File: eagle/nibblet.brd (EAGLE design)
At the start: 31.3 x 31.2 mm, 21 parts, among them IC1 MEGA8-AI

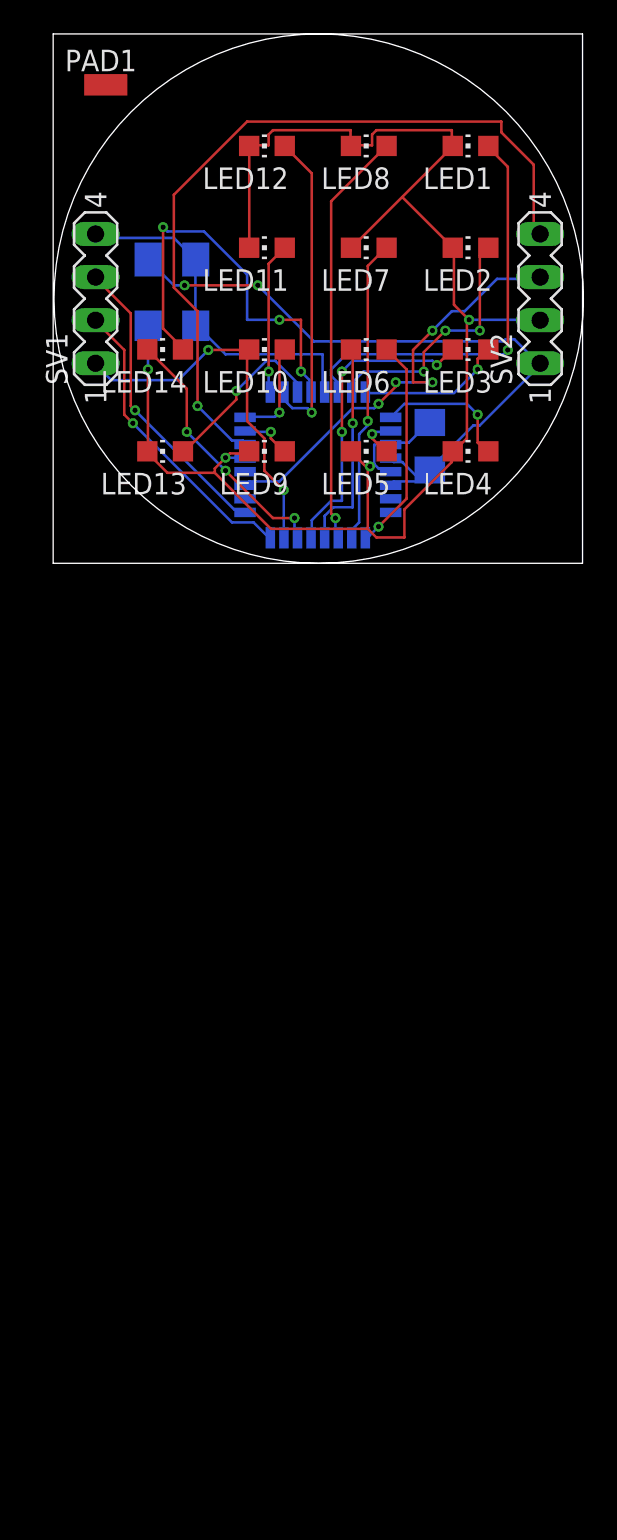
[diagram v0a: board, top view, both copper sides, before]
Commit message: add series resistors to leds
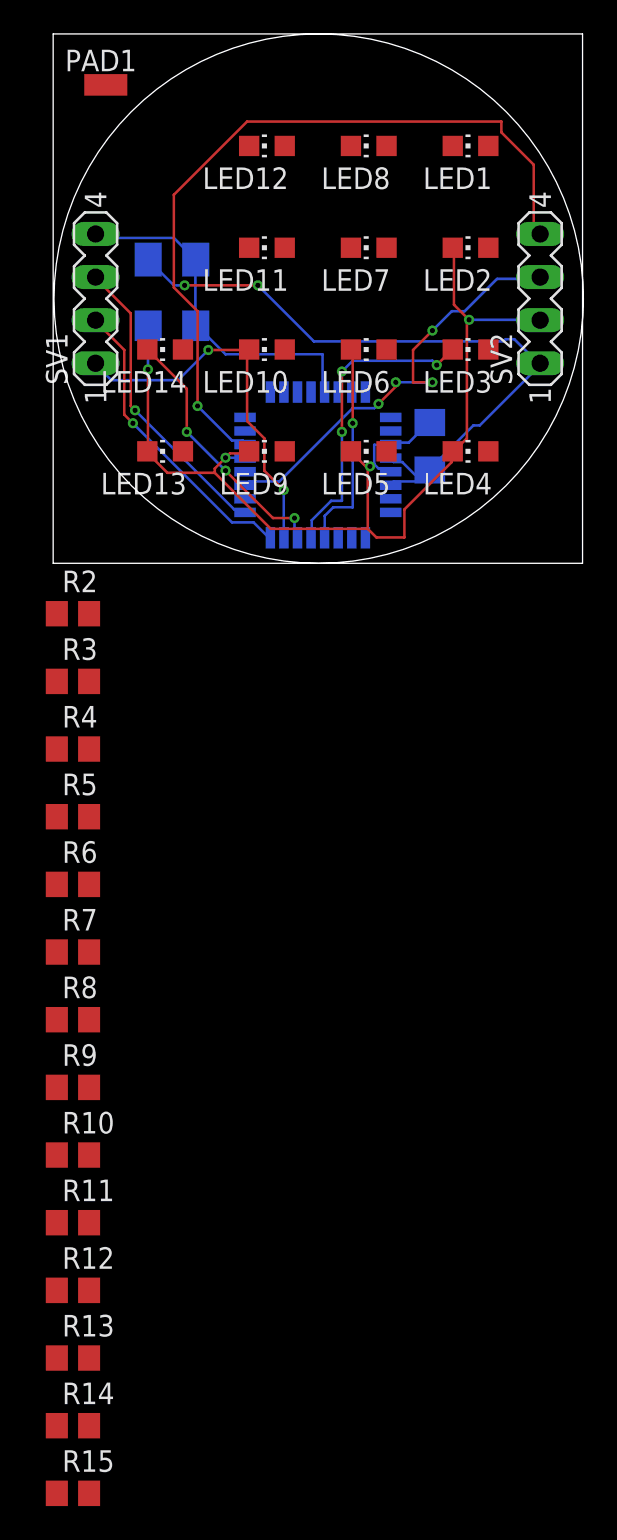
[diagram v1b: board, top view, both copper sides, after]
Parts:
- added R10, R11, R12, R13, R14, R15, R2, R3, R4, R5, R6, R7, R8, R9: (no value), rcl:R0805
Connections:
- new net N$17: IC1.11, R9.1
- new net N$18: LED8.C, R9.2
- new net N$25: LED7.C, R8.2
- new net N$26: LED6.C, R7.2
- new net N$27: LED5.C, R6.2
- new net N$28: LED4.C, R5.2
- new net N$29: LED3.C, R4.2
- new net N$30: LED2.C, R3.2
- new net N$31: LED1.C, R2.2
- new net N$32: LED13.C, R14.2
- new net N$33: IC1.28, R15.1
- new net N$34: LED14.C, R15.2
- new net N$35: LED10.C, R11.2
- new net N$36: LED9.C, R10.2
- net GND: now also LED1.A, LED11.A, LED12.A, LED13.A, LED2.A, LED4.A, LED5.A, LED7.A, LED8.A, LED9.A; no longer LED1.C, LED11.C, LED12.C, LED13.C, LED2.C, LED4.C, LED5.C, LED7.C, LED8.C, LED9.C
- net N$1: now also IC1.25, R12.1; no longer IC1.23, LED9.A
- net N$10: now also IC1.32, R4.1; no longer IC1.1, LED4.A
- net N$11: now also IC1.1, R5.1; no longer IC1.2, LED5.A
- net N$12: now also IC1.2, R6.1; no longer IC1.9, LED6.A
- net N$13: now also IC1.9, R7.1; no longer IC1.10, LED7.A
- net N$14: now also IC1.10, R8.1; no longer IC1.11, LED8.A
- net N$15: now also LED10.A; no longer LED10.C
- net N$2: now also LED11.C, R12.2; no longer IC1.24, LED10.A
- net N$20: now also LED14.A; no longer LED14.C
- net N$22: now also LED3.A; no longer LED3.C
- net N$23: now also LED6.A; no longer LED6.C
- net N$3: now also IC1.23, R10.1; no longer IC1.25, LED11.A
- net N$4: now also IC1.24, R11.1; no longer IC1.26, LED12.A
- net N$5: now also IC1.26, R13.1; no longer IC1.27, LED13.A
- net N$6: now also LED12.C, R13.2; no longer IC1.28, LED14.A
- net N$7: now also IC1.27, R14.1; no longer IC1.30, LED1.A
- net N$8: now also IC1.30, R2.1; no longer IC1.31, LED2.A
- net N$9: now also IC1.31, R3.1; no longer IC1.32, LED3.A
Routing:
- net GND: track 97.6 -> 62.7 mm
- net N$7: track 24.9 -> 0.00 mm, vias 1 -> 0
- net N$14: track 24.7 -> 0.00 mm, vias 1 -> 0
- net N$6: track 24.2 -> 0.00 mm, vias 3 -> 0
- net N$4: track 18.8 -> 0.00 mm, vias 1 -> 0
- net N$13: track 18.0 -> 0.00 mm, vias 1 -> 0
- net N$8: track 15.1 -> 0.00 mm, vias 3 -> 0
- net N$12: track 12.7 -> 0.00 mm, vias 1 -> 0
- net N$5: track 10.3 -> 0.00 mm, vias 1 -> 0
- net N$3: track 8.96 -> 0.00 mm, vias 1 -> 0
- net N$9: track 8.72 -> 0.00 mm, vias 1 -> 0
- net N$10: track 8.21 -> 0.00 mm, vias 1 -> 0
- net N$2: track 5.99 -> 0.00 mm, vias 1 -> 0
- net N$1: track 3.05 -> 0.00 mm, vias 1 -> 0
- net N$11: track 2.59 -> 0.00 mm, vias 1 -> 0

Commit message: placed resistors and autorouted 100%
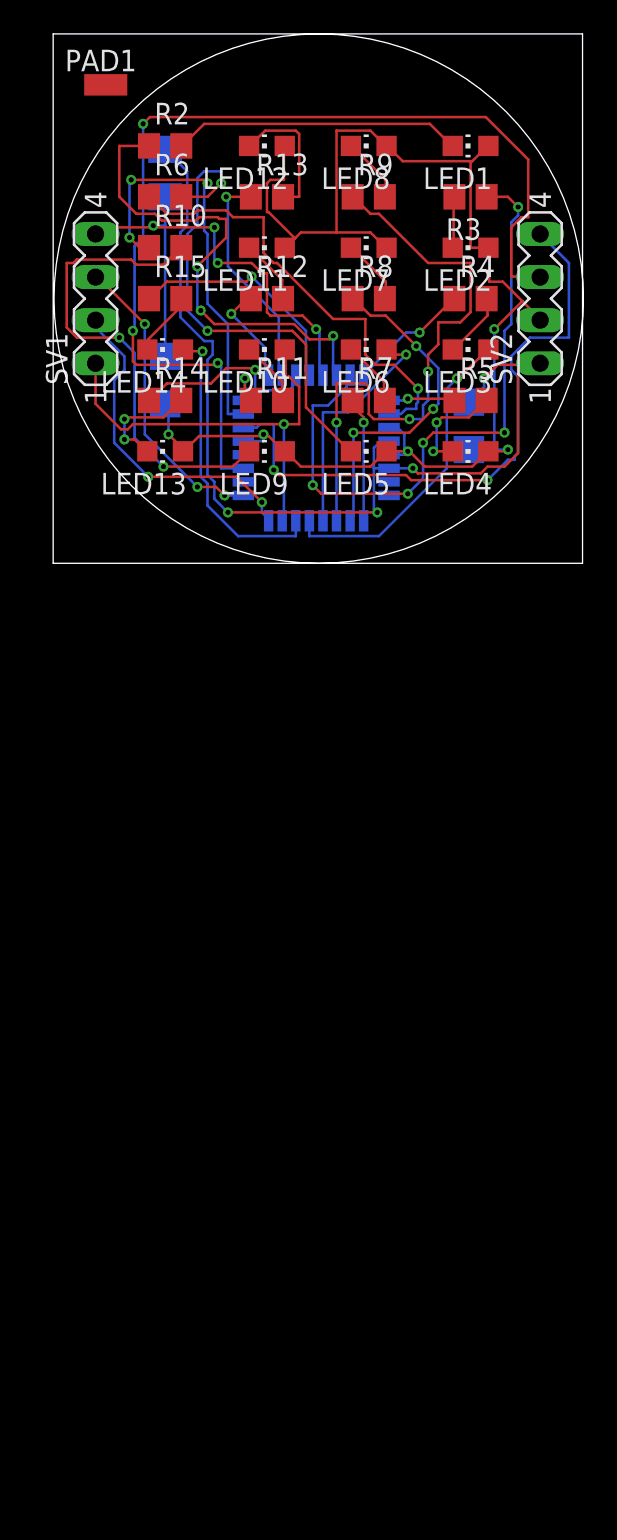
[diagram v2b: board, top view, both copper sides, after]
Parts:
- moved R15 70.6 mm to (6.60, 15.6)
- moved R13 69.4 mm to (12.6, 21.6)
- moved R14 60.7 mm to (6.60, 9.60)
- moved R12 59.6 mm to (12.6, 15.6)
- moved R9 55.3 mm to (18.6, 21.6)
- moved R10 53.7 mm to (6.60, 18.6)
- moved R11 49.8 mm to (12.6, 9.60)
- moved R8 45.9 mm to (18.6, 15.6)
- moved R6 40.9 mm to (6.60, 21.6)
- moved R3 36.9 mm to (24.6, 21.6), turned to 180 degrees
- moved R7 36.9 mm to (18.6, 9.60)
- moved R4 35.4 mm to (24.6, 15.6)
- moved R5 33.9 mm to (24.6, 9.60)
- moved R2 28.1 mm to (6.60, 24.6)
- moved R1 5.12 mm to (6.60, 23.0), turned to 270 degrees
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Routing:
- net N$9: track 0.00 -> 37.9 mm, vias 0 -> 5
- net N$17: track 0.00 -> 34.7 mm, vias 0 -> 3
- net N$19: track 26.0 -> 60.1 mm, vias 4 -> 3
- net N$8: track 0.00 -> 28.9 mm, vias 0 -> 3
- net N$36: track 0.00 -> 28.6 mm, vias 0 -> 2
- net N$27: track 0.00 -> 28.3 mm, vias 0 -> 2
- net N$12: track 0.00 -> 26.1 mm, vias 0 -> 1
- net N$3: track 0.00 -> 24.6 mm, vias 0 -> 3
- net GND: track 62.7 -> 83.6 mm, vias 4 -> 5
- net N$14: track 0.00 -> 19.8 mm, vias 0 -> 3
- net VCC: track 40.7 -> 58.7 mm, vias 2 -> 4
- net N$31: track 0.00 -> 17.1 mm
- net N$33: track 0.00 -> 13.8 mm, vias 0 -> 1
- net N$5: track 0.00 -> 13.3 mm, vias 0 -> 1
- net N$7: track 0.00 -> 11.3 mm, vias 0 -> 1
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
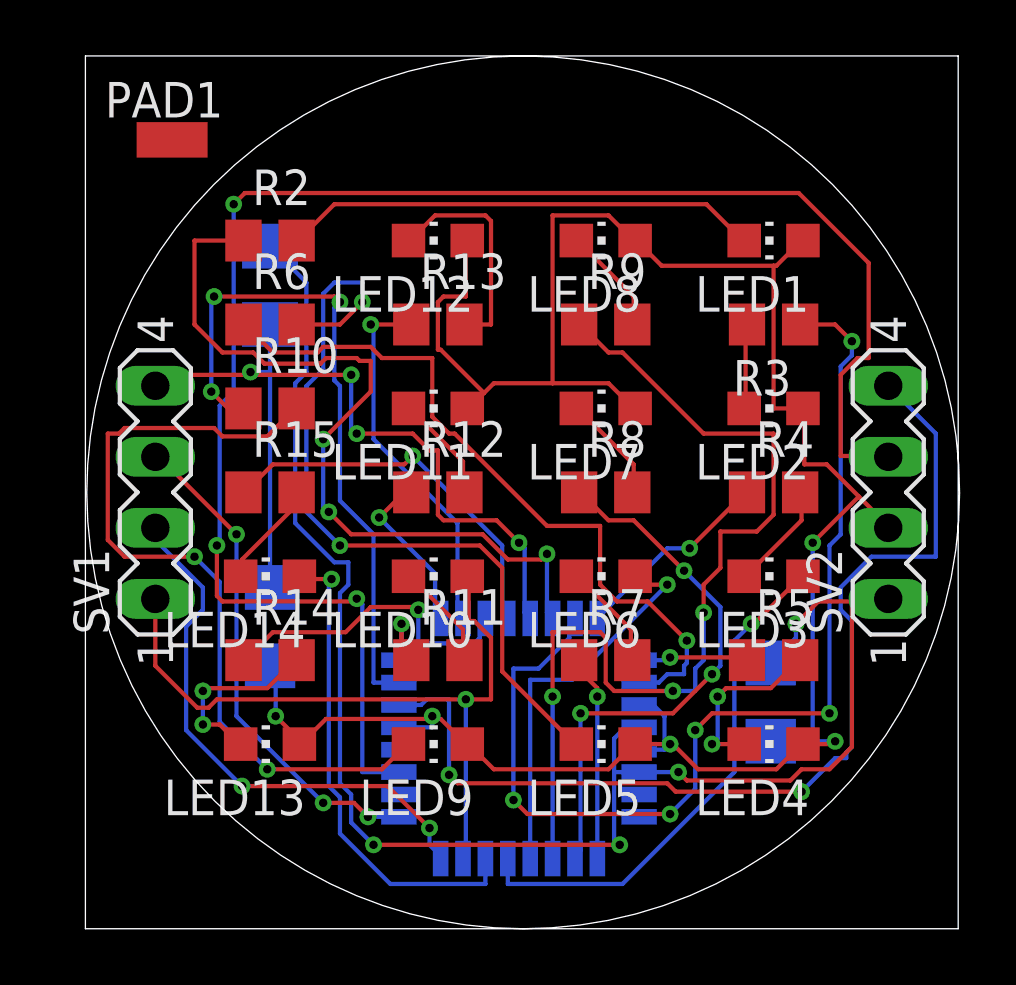
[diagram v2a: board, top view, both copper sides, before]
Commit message: consistent led order
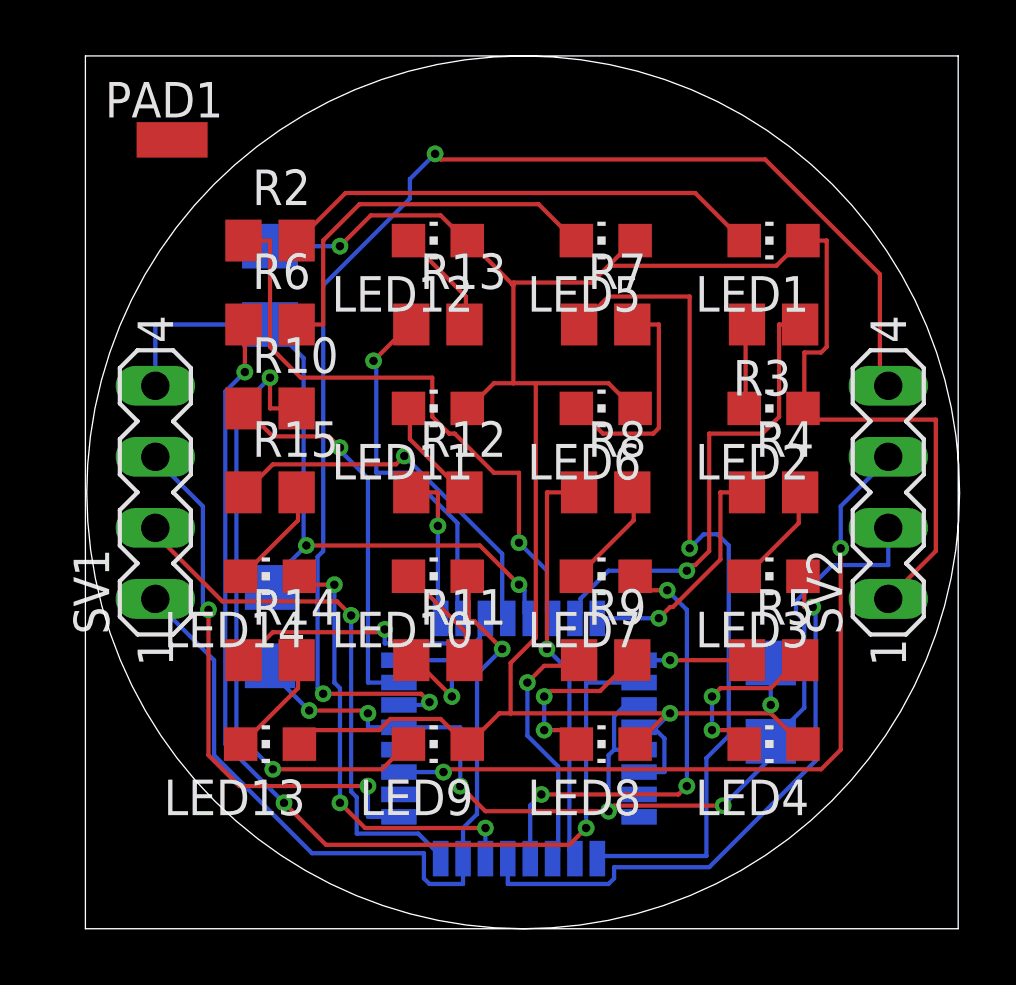
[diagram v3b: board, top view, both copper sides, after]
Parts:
- moved LED5 18.0 mm to (18.6, 24.6)
- moved LED8 18.0 mm to (18.6, 6.60)
- moved R7 12.0 mm to (18.6, 21.6)
- moved R9 12.0 mm to (18.6, 9.60)
- moved LED6 6.00 mm to (18.6, 18.6)
- moved LED7 6.00 mm to (18.6, 12.6)
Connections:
- net GND: no longer LED1.A, LED11.A, LED12.A, LED13.A, LED2.A, LED4.A, LED5.A, LED7.A, LED8.A, LED9.A
- net N$23: now also LED7.A; no longer LED6.A
- net VCC: now also LED1.A, LED11.A, LED12.A, LED13.A, LED2.A, LED4.A, LED5.A, LED6.A, LED8.A, LED9.A
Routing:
- net GND: track 83.6 -> 39.3 mm
- net VCC: track 58.7 -> 92.2 mm, vias 4 -> 3
- net N$19: track 60.1 -> 27.3 mm, vias 3 -> 2
- net N$17: track 34.7 -> 9.01 mm, vias 3 -> 1
- net N$13: track 7.39 -> 30.6 mm
- net N$9: track 37.9 -> 17.1 mm, vias 5 -> 1
- net N$27: track 28.3 -> 14.1 mm, vias 2 -> 0
- net N$16: track 36.5 -> 48.2 mm, vias 2 -> 3
- net N$12: track 26.1 -> 37.1 mm, vias 1 -> 3
- net N$3: track 24.6 -> 14.0 mm, vias 3 -> 1
- net N$8: track 28.9 -> 22.0 mm, vias 3 -> 1
- net N$36: track 28.6 -> 22.3 mm
- net N$14: track 19.8 -> 14.7 mm, vias 3 -> 1
- net N_RESET: track 31.2 -> 26.4 mm, vias 4 -> 2
- net N$15: track 25.8 -> 30.0 mm
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
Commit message: led position really consistent
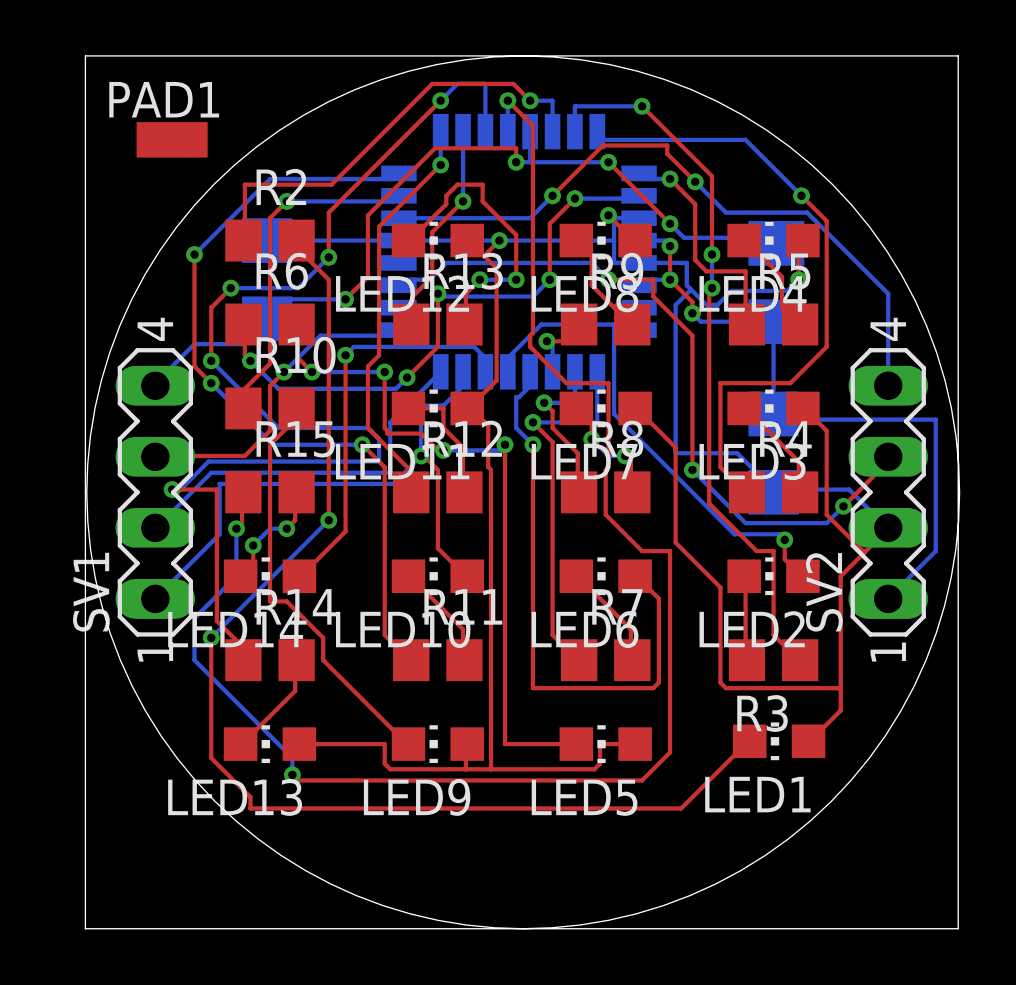
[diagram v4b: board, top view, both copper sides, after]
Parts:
- moved R1 18.1 mm to (24.7, 23.1), turned to 90 degrees
- moved LED4 18.0 mm to (24.6, 24.6)
- moved LED5 18.0 mm to (18.6, 6.60)
- moved LED8 18.0 mm to (18.6, 24.6)
- moved LED1 17.9 mm to (24.8, 6.70)
- moved IC1 17.4 mm to (15.5, 24.2)
- moved C2 12.4 mm to (6.50, 23.2), turned to 270 degrees
- moved R3 12.0 mm to (24.6, 9.60)
- moved R5 12.0 mm to (24.6, 21.6)
- moved R7 12.0 mm to (18.6, 9.60)
- moved R9 12.0 mm to (18.6, 21.6)
- moved C1 8.90 mm to (24.6, 17.0)
- moved LED2 6.00 mm to (24.6, 12.6)
- moved LED3 6.00 mm to (24.6, 18.6)
- moved LED6 6.00 mm to (18.6, 12.6)
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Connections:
- net GND: now also LED1.A, LED11.A, LED12.A, LED13.A, LED3.A, LED4.A, LED5.A, LED7.A, LED8.A, LED9.A
- net N$22: now also LED2.A; no longer LED3.A
- net N$23: now also LED6.A; no longer LED7.A
- net VCC: no longer LED1.A, LED11.A, LED12.A, LED13.A, LED2.A, LED4.A, LED5.A, LED6.A, LED8.A, LED9.A
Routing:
- net GND: track 39.3 -> 107.2 mm, vias 5 -> 3
- net VCC: track 92.2 -> 24.5 mm
- net N$33: track 13.6 -> 54.9 mm, vias 1 -> 3
- net N$7: track 10.3 -> 41.6 mm, vias 1 -> 5
- net N$31: track 17.4 -> 42.0 mm, vias 0 -> 2
- net N$16: track 48.2 -> 24.2 mm, vias 3 -> 2
- net N$4: track 5.18 -> 28.1 mm, vias 1 -> 3
- net N$13: track 30.6 -> 13.3 mm
- net N$12: track 37.1 -> 21.0 mm, vias 3 -> 5
- net N$10: track 8.63 -> 22.7 mm
- net N$27: track 14.1 -> 24.6 mm, vias 0 -> 4
- net N$1: track 5.50 -> 14.6 mm
- net N$9: track 17.1 -> 25.9 mm, vias 1 -> 3
- net N$14: track 14.7 -> 5.95 mm
- net N$21: track 19.8 -> 11.5 mm, vias 2 -> 1
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
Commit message: pad for battery. GND on the PCB??
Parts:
- added PAD2, PAD3: WIREPADSMD1,27-254, wirepad:SMD1,27-2,54
- moved PAD1 22.5 mm to (14.3, 8.70), flipped to the bottom
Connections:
- net GND: now also PAD1.1, PAD2.1, PAD3.1
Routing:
- net GND: track 107.2 -> 125.6 mm
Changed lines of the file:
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@@
 <?xml version="1.0" encoding="utf-8"?>
 <!DOCTYPE eagle SYSTEM "eagle.dtd">
-<eagle version="6.4">
+<eagle version="6.5.0">
 <drawing>
 <settings>
@@
 <layer number="19" name="Unrouted" color="6" fill="1" visible="yes" active="yes"/>
 <layer number="20" name="Dimension" color="15" fill="1" visible="yes" active="yes"/>
-<layer number="21" name="tPlace" color="7" fill="1" visible="yes" active="yes"/>
+<layer number="21" name="tPlace" color="7" fill="1" visible="no" active="yes"/>
 <layer number="22" name="bPlace" color="7" fill="1" visible="yes" active="yes"/>
 <layer number="23" name="tOrigins" color="15" fill="1" visible="no" active="yes"/>
 <layer number="24" name="bOrigins" color="15" fill="1" visible="yes" active="yes"/>
-<layer number="25" name="tNames" color="7" fill="1" visible="yes" active="yes"/>
+<layer number="25" name="tNames" color="7" fill="1" visible="no" active="yes"/>
 <layer number="26" name="bNames" color="7" fill="1" visible="no" active="yes"/>
 <layer number="27" name="tValues" color="7" fill="1" visible="no" active="yes"/>
@@
 <element name="C1" library="rcl" package="C1206" value="" x="24.6" y="17" rot="MR90"/>
 <element name="C2" library="rcl" package="C1206" value="" x="6.5" y="23.2" rot="MR270"/>
-<element name="PAD1" library="wirepad" package="SMD1,27-2,54" value="WIREPADSMD1,27-254" x="3.1" y="28.2" rot="R270"/>
+<element name="PAD1" library="wirepad" package="SMD1,27-2,54" value="WIREPADSMD1,27-254" x="14.3" y="8.7" rot="MR270"/>
 <element name="SV1" library="con-lstb" package="MA04-1" value="" x="2.5" y="15.6" rot="R90"/>
 <element name="SV2" library="con-lstb" package="MA04-1" value="" x="28.7" y="15.6" rot="R90"/>
@@
 <element name="R14" library="rcl" package="R0805" value="" x="6.6" y="9.6"/>
 <element name="R15" library="rcl" package="R0805" value="" x="6.6" y="15.6"/>
+<element name="PAD2" library="wirepad" package="SMD1,27-2,54" value="WIREPADSMD1,27-254" x="16.4" y="7.8" rot="MR150"/>
+<element name="PAD3" library="wirepad" package="SMD1,27-2,54" value="WIREPADSMD1,27-254" x="16.4" y="9.8" rot="MR30"/>
 </elements>
 <signals>
@@
 <via x="25.5" y="23.2" extent="1-16" drill="0.3"/>
 <via x="14.8" y="24.6" extent="1-16" drill="0.3"/>
+<contactref element="PAD1" pad="1"/>
+<contactref element="PAD3" pad="1"/>
+<contactref element="PAD2" pad="1"/>
+<wire x1="16.4" y1="9.8" x2="16.8" y2="10.2" width="0.4064" layer="16"/>
+<wire x1="16.8" y1="10.2" x2="16.8" y2="10.6" width="0.4064" layer="16"/>
+<wire x1="16.8" y1="10.6" x2="18.9" y2="12.7" width="0.4064" layer="16"/>
+<wire x1="18.9" y1="12.7" x2="26.1" y2="12.7" width="0.4064" layer="16"/>
+<wire x1="26.1" y1="12.7" x2="27.73" y2="14.33" width="0.4064" layer="16"/>
+<wire x1="27.73" y1="14.33" x2="28.7" y2="14.33" width="0.4064" layer="16"/>
+<wire x1="16.4" y1="9.8" x2="15.7" y2="9.1" width="0.4064" layer="16"/>
+<wire x1="15.7" y1="9.1" x2="15.7" y2="8.7" width="0.4064" layer="16"/>
+<wire x1="15.7" y1="8.7" x2="16.4" y2="8" width="0.4064" layer="16"/>
+<wire x1="16.4" y1="8" x2="16.4" y2="7.8" width="0.4064" layer="16"/>
+<wire x1="14.3" y1="8.7" x2="15.7" y2="8.7" width="0.4064" layer="16"/>
 </signal>
 <signal name="N$19">
